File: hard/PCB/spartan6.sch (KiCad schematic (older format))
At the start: 26 parts, among them IC1 W9812G6KH, J1 HDMI_A, SW1 B3SL-1002P, X1 ASV-32.000MHZ-E-T

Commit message: Update supply power
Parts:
- removed PIO1, PIO2: CONN_02X10, Socket_Strips:Socket_Strip_Straight_2x10_Pitch2.54mm, symbol CONN_02X10
- added GIO1, GIO2: CONN_01X07, Pin_Headers:Pin_Header_Straight_1x07_Pitch2.54mm, symbol CONN_01X07
- DF1, DF2: footprint opendous:SM0603 -> LEDs:LED_0603
- IC1: footprint opendous:TSOPII54_SDRAM_MT48 -> Project:TSOPII54_SDRAM_MT48
- J1: footprint HDMI:FCI_10029449-11[13]RLF -> Project:HDMI_FCI_10029449-11[13]RLF
- RF1, RF3, RF4, RF8: footprint opendous:SM0603 -> Resistors_SMD:R_0603
- RF2: value 4.7k -> 68; footprint opendous:SM0603 -> Resistors_SMD:R_0603
- RF5: value 1k -> 68; footprint opendous:SM0603 -> Resistors_SMD:R_0603
- RF6: value 68 -> 4.7k; footprint opendous:SM0603 -> Resistors_SMD:R_0603
- RF7: value 68 -> 1k; footprint opendous:SM0603 -> Resistors_SMD:R_0603
- U1: renamed from UF1; footprint Housings_QFP:LQFP-144_20x20mm_Pitch0.5mm -> Project:LQFP-144_20x20mm_Pitch0.5mm
- X1: footprint opendous:OSCILLATOR_7x5mm -> Project:OSCILLATOR_7x5mm
- renumbered SW1 to RST1
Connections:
- net labels added: CS_AD, DA0, DA1, DA2, DA3, DA4, DA5, DA6, DA7, DA[0..7], DD0, DD1, DD2, DD3, DD4, DD5, DD6, DD7, DD8, DD9, DD[0..9], FPGA_CK, LED1, LED2, SPI_MOSI, SPI_SCK
- net labels removed: +5V, F_~SD
- wire segments 243 -> 255
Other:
- moved on the sheet: DF1, IC1, J1, LVDS1, R10, R11, R4, R5, R6, R7, R8, R9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

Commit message: Corrección esquematico
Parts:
- removed R10, R11, R5, R6, R7, R8, R9: 51, Resistors_SMD:R_0402, symbol R
- removed RF2, RF3, RF5: 68, Resistors_SMD:R_0603, symbol R
- removed RF8: 1k, Resistors_SMD:R_0603, symbol R
- added RH2, RH3, RH4, RH5, RH6, RH7, RH8: 51, Resistors_SMD:R_0402, symbol R
- added RS2: 1k, Resistors_SMD:R_0603, symbol R
- added RS4, RS5, RS6: 68, Resistors_SMD:R_0603, symbol R
- renumbered DF2 to DS1, DF1 to DS2, J1 to HDMI1, R4 to RH1, RF1 to RR1, RF7 to RS1, RF4 to RS3, RF6 to RS7, X1 to XS1
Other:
- moved on the sheet: HDMI1, IC1, LVDS1, RH1

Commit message: Add 3d model
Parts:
- removed GIO1, GIO2: CONN_01X07, Pin_Headers:Pin_Header_Straight_1x07_Pitch2.54mm, symbol CONN_01X07
- added P?: CONN_02X20, symbol CONN_02X20
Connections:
- net labels added: +3.3V, RXD, SCL, SDA, SPI_MISO, TXD, VDD5V
- wire segments 255 -> 297
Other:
- note added: "REVISAR!!!!!"

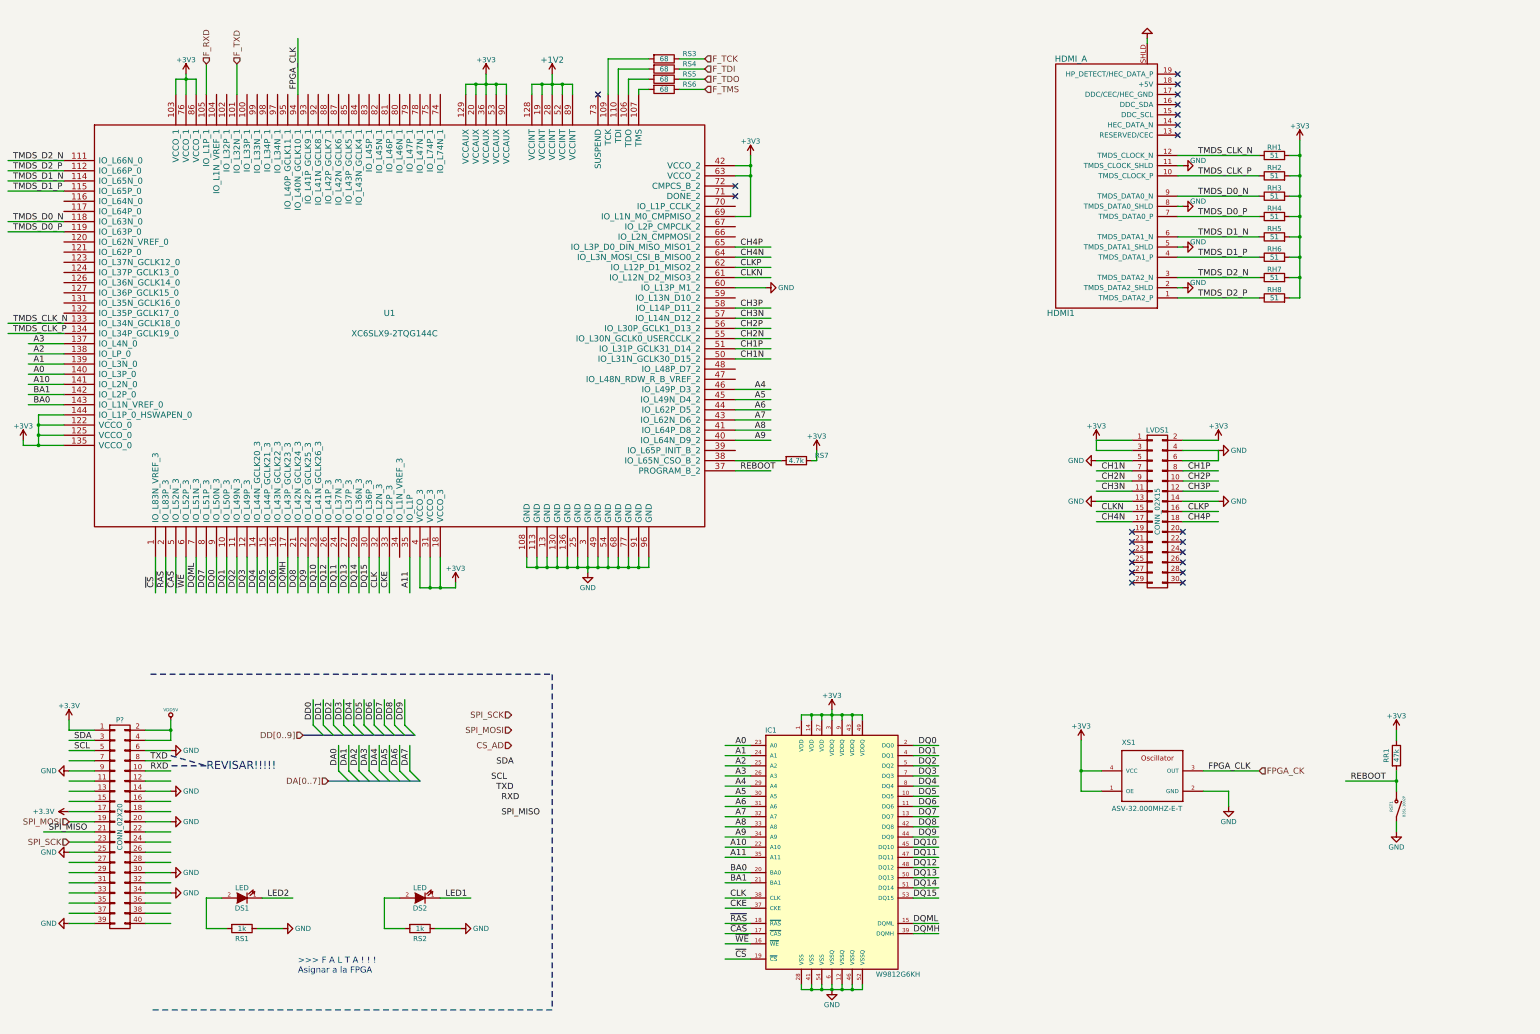
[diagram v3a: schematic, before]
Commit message: update 3d models
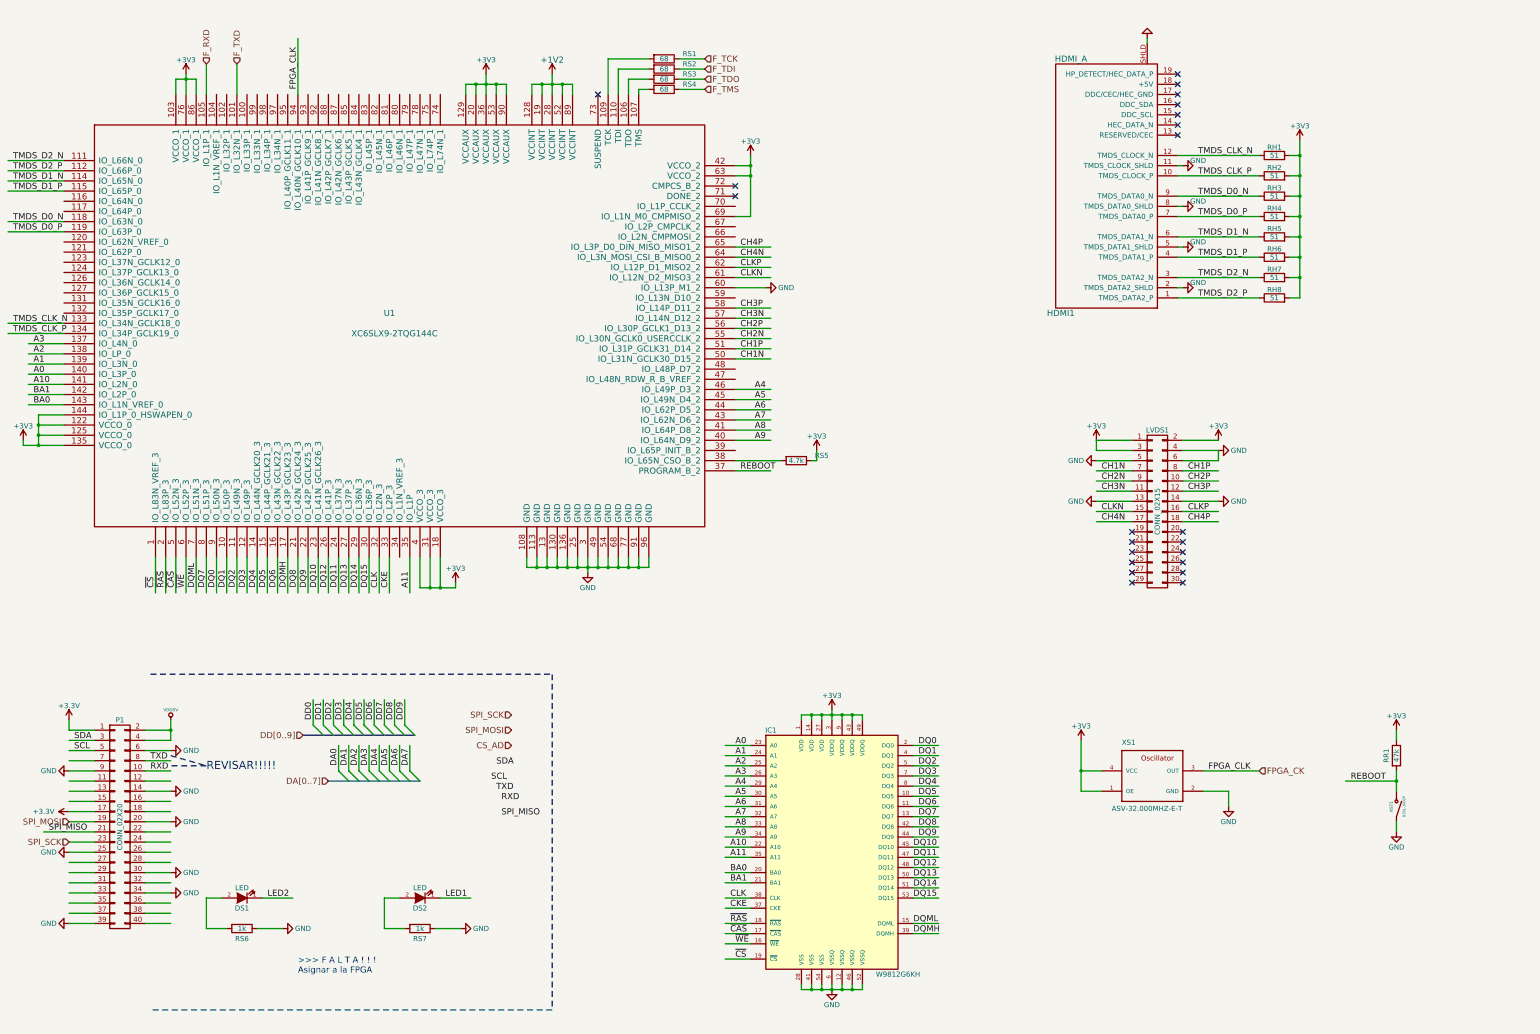
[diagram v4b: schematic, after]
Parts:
- P1: renamed from P?; footprint (none) -> Pin_Headers:Pin_Header_Straight_2x20_Pitch2.54mm
- renumbered RS3 to RS1, RS4 to RS2, RS5 to RS3, RS6 to RS4, RS7 to RS5, RS1 to RS6, RS2 to RS7

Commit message: update layout
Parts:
- removed LVDS1: CONN_02X15, Pin_Headers:Pin_Header_Straight_2x15_Pitch2.00mm, symbol CONN_02X15
- added LVDS1: CONN_02X09, Project:LVDS_SMD, symbol CONN_02X09
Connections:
- net labels removed: +3.3V
- wire segments 297 -> 295
- no-connect marks 22 -> 12
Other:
- note added: "+3v3 Rpi"

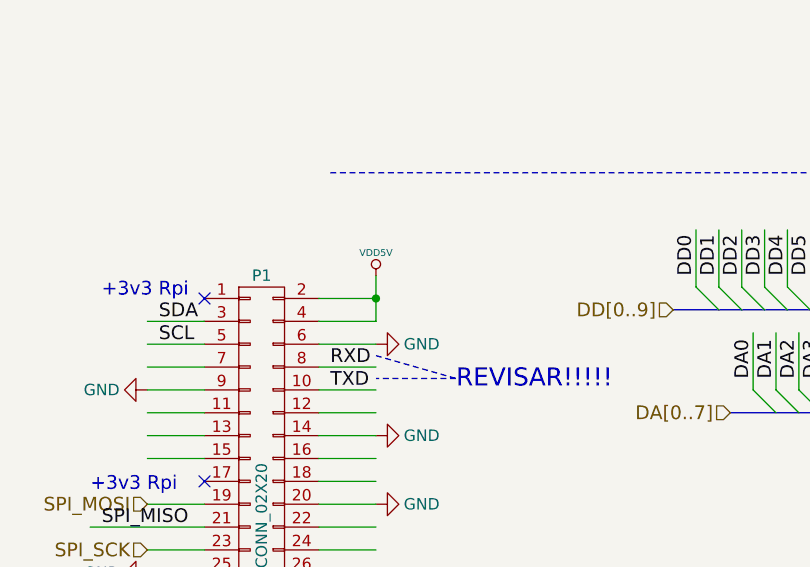
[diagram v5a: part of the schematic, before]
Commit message: Add jmp Rpi Power
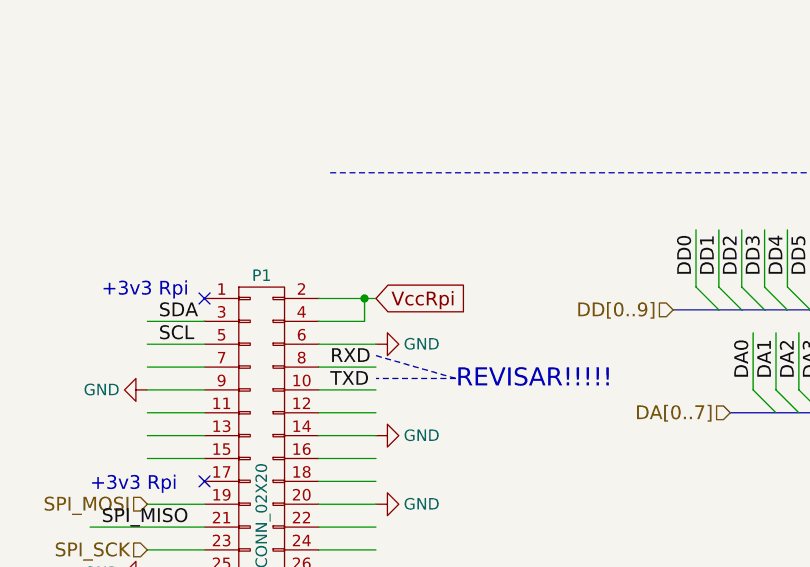
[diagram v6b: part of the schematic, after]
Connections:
- net labels added: VccRpi
- net labels removed: VDD5V
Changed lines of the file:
@@
 $EndComp
 $Comp
-L +1V2 #PWR019
+L +1V2 #PWR22
 U 1 1 54C59A64
 P 6600 1550
-F 0 "#PWR019" H 6600 1400 60  0001 C CNN
+F 0 "#PWR22" H 6600 1400 60  0001 C CNN
 F 1 "+1V2" H 6600 1690 60  0000 C CNN
 F 2 "" H 6600 1550 60  0000 C CNN
@@
 $EndComp
 $Comp
-L +3V3 #PWR020
+L +3V3 #PWR30
 U 1 1 589C6271
 P 1400 5150
-F 0 "#PWR020" H 1400 5000 50  0001 C CNN
+F 0 "#PWR30" H 1400 5000 50  0001 C CNN
 F 1 "+3V3" H 1400 5290 50  0000 C CNN
 F 2 "" H 1400 5150 50  0000 C CNN
@@
 $EndComp
 $Comp
-L +3V3 #PWR021
+L +3V3 #PWR20
 U 1 1 589C75F3
 P 3000 1550
-F 0 "#PWR021" H 3000 1400 50  0001 C CNN
+F 0 "#PWR20" H 3000 1400 50  0001 C CNN
 F 1 "+3V3" H 3000 1690 50  0000 C CNN
 F 2 "" H 3000 1550 50  0000 C CNN
@@
 $EndComp
 $Comp
-L +3V3 #PWR022
+L +3V3 #PWR21
 U 1 1 589CF003
 P 5950 1550
-F 0 "#PWR022" H 5950 1400 50  0001 C CNN
+F 0 "#PWR21" H 5950 1400 50  0001 C CNN
 F 1 "+3V3" H 5950 1690 50  0000 C CNN
 F 2 "" H 5950 1550 50  0000 C CNN
@@
 $EndComp
 $Comp
-L +3V3 #PWR023
+L +3V3 #PWR24
 U 1 1 589D05F4
 P 8550 2350
-F 0 "#PWR023" H 8550 2200 50  0001 C CNN
+F 0 "#PWR24" H 8550 2200 50  0001 C CNN
 F 1 "+3V3" H 8550 2490 50  0000 C CNN
 F 2 "" H 8550 2350 50  0000 C CNN
@@
 $EndComp
 $Comp
-L +3V3 #PWR024
+L +3V3 #PWR33
 U 1 1 589D22FF
 P 9200 5250
-F 0 "#PWR024" H 9200 5100 50  0001 C CNN
+F 0 "#PWR33" H 9200 5100 50  0001 C CNN
 F 1 "+3V3" H 9200 5390 50  0000 C CNN
 F 2 "" H 9200 5250 50  0000 C CNN
@@
 $EndComp
 $Comp
-L +3V3 #PWR025
+L +3V3 #PWR39
 U 1 1 589D4A17
 P 5650 6550
-F 0 "#PWR025" H 5650 6400 50  0001 C CNN
+F 0 "#PWR39" H 5650 6400 50  0001 C CNN
 F 1 "+3V3" H 5650 6690 50  0000 C CNN
 F 2 "" H 5650 6550 50  0000 C CNN
@@
 $EndComp
 $Comp
-L +3V3 #PWR026
+L +3V3 #PWR42
 U 1 1 589DBA37
 P 11800 8100
-F 0 "#PWR026" H 11800 7950 50  0001 C CNN
+F 0 "#PWR42" H 11800 7950 50  0001 C CNN
 F 1 "+3V3" H 11800 8240 50  0000 C CNN
 F 2 "" H 11800 8100 50  0000 C CNN
@@
 $EndComp
 $Comp
-L +3V3 #PWR027
+L +3V3 #PWR40
 U 1 1 589DD066
 P 9350 7800
-F 0 "#PWR027" H 9350 7650 50  0001 C CNN
+F 0 "#PWR40" H 9350 7650 50  0001 C CNN
 F 1 "+3V3" H 9350 7940 50  0000 C CNN
 F 2 "" H 9350 7800 50  0000 C CNN
@@
 $EndComp
 $Comp
-L +3V3 #PWR028
+L +3V3 #PWR23
 U 1 1 589DF268
 P 13950 2200
-F 0 "#PWR028" H 13950 2050 50  0001 C CNN
+F 0 "#PWR23" H 13950 2050 50  0001 C CNN
 F 1 "+3V3" H 13950 2340 50  0000 C CNN
 F 2 "" H 13950 2200 50  0000 C CNN
@@
 $EndComp
 $Comp
-L +3V3 #PWR029
+L +3V3 #PWR32
 U 1 1 589E24D4
 P 13150 5150
-F 0 "#PWR029" H 13150 5000 50  0001 C CNN
+F 0 "#PWR32" H 13150 5000 50  0001 C CNN
 F 1 "+3V3" H 13150 5290 50  0000 C CNN
 F 2 "" H 13150 5150 50  0000 C CNN
@@
 CLKP
 $Comp
-L +3V3 #PWR030
+L +3V3 #PWR31
 U 1 1 58A0DAEA
 P 11950 5150
-F 0 "#PWR030" H 11950 5000 50  0001 C CNN
+F 0 "#PWR31" H 11950 5000 50  0001 C CNN
 F 1 "+3V3" H 11950 5290 50  0000 C CNN
 F 2 "" H 11950 5150 50  0000 C CNN
@@
 REBOOT
 $Comp
-L +3V3 #PWR031
+L +3V3 #PWR41
 U 1 1 58A59A51
 P 14900 8000
-F 0 "#PWR031" H 14900 7850 50  0001 C CNN
+F 0 "#PWR41" H 14900 7850 50  0001 C CNN
 F 1 "+3V3" H 14900 8140 50  0000 C CNN
 F 2 "" H 14900 8000 50  0000 C CNN
@@
 $EndComp
 $Comp
-L GND #PWR032
+L GND #PWR28
 U 1 1 592E08F7
 P 8700 3650
-F 0 "#PWR032" H 8700 3400 50  0001 C CNN
+F 0 "#PWR28" H 8700 3400 50  0001 C CNN
 F 1 "GND" V 8700 3450 50  0000 C CNN
 F 2 "" H 8700 3650 50  0000 C CNN
@@
 $EndComp
 $Comp
-L GND #PWR033
+L GND #PWR26
 U 1 1 592E1225
 P 12800 2850
-F 0 "#PWR033" H 12800 2600 50  0001 C CNN
+F 0 "#PWR26" H 12800 2600 50  0001 C CNN
 F 1 "GND" V 12850 2700 50  0000 C CNN
 F 2 "" H 12800 2850 50  0000 C CNN
@@
 $EndComp
 $Comp
-L GND #PWR034
+L GND #PWR38
 U 1 1 592E17AE
 P 6950 6450
-F 0 "#PWR034" H 6950 6200 50  0001 C CNN
+F 0 "#PWR38" H 6950 6200 50  0001 C CNN
 F 1 "GND" H 6950 6300 50  0000 C CNN
 F 2 "" H 6950 6450 50  0000 C CNN
@@
 $EndComp
 $Comp
-L GND #PWR035
+L GND #PWR25
 U 1 1 592E289B
 P 12800 2450
-F 0 "#PWR035" H 12800 2200 50  0001 C CNN
+F 0 "#PWR25" H 12800 2200 50  0001 C CNN
 F 1 "GND" V 12850 2300 50  0000 C CNN
 F 2 "" H 12800 2450 50  0000 C CNN
@@
 $EndComp
 $Comp
-L GND #PWR036
+L GND #PWR29
 U 1 1 592E2A16
 P 12800 3650
-F 0 "#PWR036" H 12800 3400 50  0001 C CNN
+F 0 "#PWR29" H 12800 3400 50  0001 C CNN
 F 1 "GND" V 12850 3500 50  0000 C CNN
 F 2 "" H 12800 3650 50  0000 C CNN
@@
 $EndComp
 $Comp
-L GND #PWR037
+L GND #PWR27
 U 1 1 592E2AC7
 P 12800 3250
-F 0 "#PWR037" H 12800 3000 50  0001 C CNN
+F 0 "#PWR27" H 12800 3000 50  0001 C CNN
 F 1 "GND" V 12850 3100 50  0000 C CNN
 F 2 "" H 12800 3250 50  0000 C CNN
@@
 $EndComp
 $Comp
-L GND #PWR038
+L GND #PWR36
 U 1 1 592E3202
 P 11950 5750
-F 0 "#PWR038" H 11950 5500 50  0001 C CNN
+F 0 "#PWR36" H 11950 5500 50  0001 C CNN
 F 1 "GND" V 11950 5550 50  0000 C CNN
 F 2 "" H 11950 5750 50  0000 C CNN
@@
 $EndComp
 $Comp
-L GND #PWR039
+L GND #PWR34
 U 1 1 592E3582
 P 13150 5250
-F 0 "#PWR039" H 13150 5000 50  0001 C CNN
+F 0 "#PWR34" H 13150 5000 50  0001 C CNN
 F 1 "GND" V 13150 5050 50  0000 C CNN
 F 2 "" H 13150 5250 50  0000 C CNN
@@
 $EndComp
 $Comp
-L GND #PWR040
+L GND #PWR37
 U 1 1 592E362C
 P 13150 5750
-F 0 "#PWR040" H 13150 5500 50  0001 C CNN
+F 0 "#PWR37" H 13150 5500 50  0001 C CNN
 F 1 "GND" V 13150 5550 50  0000 C CNN
 F 2 "" H 13150 5750 50  0000 C CNN
@@
 $EndComp
 $Comp
-L GND #PWR041
+L GND #PWR35
 U 1 1 592E37A9
 P 11950 5350
-F 0 "#PWR041" H 11950 5100 50  0001 C CNN
+F 0 "#PWR35" H 11950 5100 50  0001 C CNN
 F 1 "GND" V 11950 5150 50  0000 C CNN
 F 2 "" H 11950 5350 50  0000 C CNN
@@
 $EndComp
 $Comp
-L GND #PWR042
+L GND #PWR48
 U 1 1 592E4258
 P 14900 9000
-F 0 "#PWR042" H 14900 8750 50  0001 C CNN
+F 0 "#PWR48" H 14900 8750 50  0001 C CNN
 F 1 "GND" H 14900 8850 50  0000 C CNN
 F 2 "" H 14900 9000 50  0000 C CNN
@@
 $EndComp
 $Comp
-L GND #PWR043
+L GND #PWR46
 U 1 1 592E438D
 P 13250 8750
-F 0 "#PWR043" H 13250 8500 50  0001 C CNN
+F 0 "#PWR46" H 13250 8500 50  0001 C CNN
 F 1 "GND" H 13250 8600 50  0000 C CNN
 F 2 "" H 13250 8750 50  0000 C CNN
@@
 $EndComp
 $Comp
-L GND #PWR044
+L GND #PWR55
 U 1 1 592E4587
 P 9350 10550
-F 0 "#PWR044" H 9350 10300 50  0001 C CNN
+F 0 "#PWR55" H 9350 10300 50  0001 C CNN
 F 1 "GND" H 9350 10400 50  0000 C CNN
 F 2 "" H 9350 10550 50  0000 C CNN
@@
 $EndComp
 $Comp
-L GND #PWR045
+L GND #PWR53
 U 1 1 592E569C
 P 3950 9950
-F 0 "#PWR045" H 3950 9700 50  0001 C CNN
+F 0 "#PWR53" H 3950 9700 50  0001 C CNN
 F 1 "GND" V 3950 9750 50  0000 C CNN
 F 2 "" H 3950 9950 50  0000 C CNN
@@
 $EndComp
 $Comp
-L GND #PWR046
+L GND #PWR54
 U 1 1 592E5C97
 P 5700 9950
-F 0 "#PWR046" H 5700 9700 50  0001 C CNN
+F 0 "#PWR54" H 5700 9700 50  0001 C CNN
 F 1 "GND" V 5700 9750 50  0000 C CNN
 F 2 "" H 5700 9950 50  0000 C CNN
@@
 SPI_MOSI
 $Comp
-L GND #PWR047
+L GND #PWR43
 U 1 1 592F3AF1
 P 2850 8200
-F 0 "#PWR047" H 2850 7950 50  0001 C CNN
+F 0 "#PWR43" H 2850 7950 50  0001 C CNN
 F 1 "GND" V 2850 8000 50  0000 C CNN
 F 2 "" H 2850 8200 50  0000 C CNN
@@
 $EndComp
 $Comp
-L GND #PWR048
+L GND #PWR45
 U 1 1 592F3B47
 P 2850 8600
-F 0 "#PWR048" H 2850 8350 50  0001 C CNN
+F 0 "#PWR45" H 2850 8350 50  0001 C CNN
 F 1 "GND" V 2850 8400 50  0000 C CNN
 F 2 "" H 2850 8600 50  0000 C CNN
@@
 $EndComp
 $Comp
-L GND #PWR049
+L GND #PWR50
 U 1 1 592F3B9D
 P 2850 9400
-F 0 "#PWR049" H 2850 9150 50  0001 C CNN
+F 0 "#PWR50" H 2850 9150 50  0001 C CNN
 F 1 "GND" V 2850 9200 50  0000 C CNN
 F 2 "" H 2850 9400 50  0000 C CNN
@@
 $EndComp
 $Comp
-L GND #PWR050
+L GND #PWR47
 U 1 1 592F3BF3
 P 2850 8900
-F 0 "#PWR050" H 2850 8650 50  0001 C CNN
+F 0 "#PWR47" H 2850 8650 50  0001 C CNN
 F 1 "GND" V 2850 8700 50  0000 C CNN
 F 2 "" H 2850 8900 50  0000 C CNN
@@
 $EndComp
 $Comp
-L GND #PWR051
+L GND #PWR51
 U 1 1 592F3C7C
 P 2850 9600
-F 0 "#PWR051" H 2850 9350 50  0001 C CNN
+F 0 "#PWR51" H 2850 9350 50  0001 C CNN
 F 1 "GND" V 2850 9400 50  0000 C CNN
 F 2 "" H 2850 9600 50  0000 C CNN
@@
 $EndComp
 $Comp
-L GND #PWR052
+L GND #PWR44
 U 1 1 592F3D27
 P 1850 8400
-F 0 "#PWR052" H 1850 8150 50  0001 C CNN
+F 0 "#PWR44" H 1850 8150 50  0001 C CNN
 F 1 "GND" V 1850 8200 50  0000 C CNN
 F 2 "" H 1850 8400 50  0000 C CNN
@@
 $EndComp
 $Comp
-L GND #PWR053
+L GND #PWR49
 U 1 1 592F3E42
 P 1850 9200
-F 0 "#PWR053" H 1850 8950 50  0001 C CNN
+F 0 "#PWR49" H 1850 8950 50  0001 C CNN
 F 1 "GND" V 1850 9000 50  0000 C CNN
 F 2 "" H 1850 9200 50  0000 C CNN
@@
 	0    1    1    0
 $EndComp
-$Comp
-L VDD5V #PWR054
-U 1 1 592F99D4
-P 2850 7900
-F 0 "#PWR054" H 2850 8000 30  0001 C CNN
-F 1 "VDD5V" H 2850 8000 30  0000 C CNN
-F 2 "" H 2850 7900 60  0001 C CNN
-F 3 "" H 2850 7900 60  0001 C CNN
-	1    2850 7900
-	1    0    0    -1
-$EndComp
 Wire Wire Line
 	2100 8100 1850 8100
@@
 Wire Wire Line
 	2850 8200 2600 8200
-Wire Wire Line
-	2850 8100 2600 8100
 Wire Wire Line
 	2850 8300 2600 8300
@@
 Wire Wire Line
 	2600 8000 2850 8000
-Wire Wire Line
-	2850 7900 2850 8100
-Connection ~ 2850 8000
 Text Label 2650 8400 0    60   ~ 0
 TXD
@@
 SCL
 $Comp
-L GND #PWR056
+L GND #PWR52
 U 1 1 59301241
 P 1850 9900
-F 0 "#PWR056" H 1850 9650 50  0001 C CNN
+F 0 "#PWR52" H 1850 9650 50  0001 C CNN
 F 1 "GND" V 1850 9700 50  0000 C CNN
 F 2 "" H 1850 9900 50  0000 C CNN
@@
 $EndComp
 $Comp
-L GND #PWR057
+L GND #PWR19
 U 1 1 5930CFAC
 P 12700 1200
-F 0 "#PWR057" H 12700 950 50  0001 C CNN
+F 0 "#PWR19" H 12700 950 50  0001 C CNN
 F 1 "GND" V 12700 1000 50  0000 C CNN
 F 2 "" H 12700 1200 50  0000 C CNN
@@
 Text Notes 1600 8850 0    60   ~ 0
 +3v3 Rpi
+Text GLabel 2850 8000 2    60   Input ~ 0
+VccRpi
+Wire Wire Line
+	2600 8100 2800 8100
+Wire Wire Line
+	2800 8100 2800 8000
+Connection ~ 2800 8000
 $EndSCHEMATC
